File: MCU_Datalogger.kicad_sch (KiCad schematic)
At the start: 25 parts, among them U1 24LC1025, U2 DS1337S_, U3 24LC1025, U4 ATMEGA328P-AU, Y1 32.768 KHz, Y2 16MHz

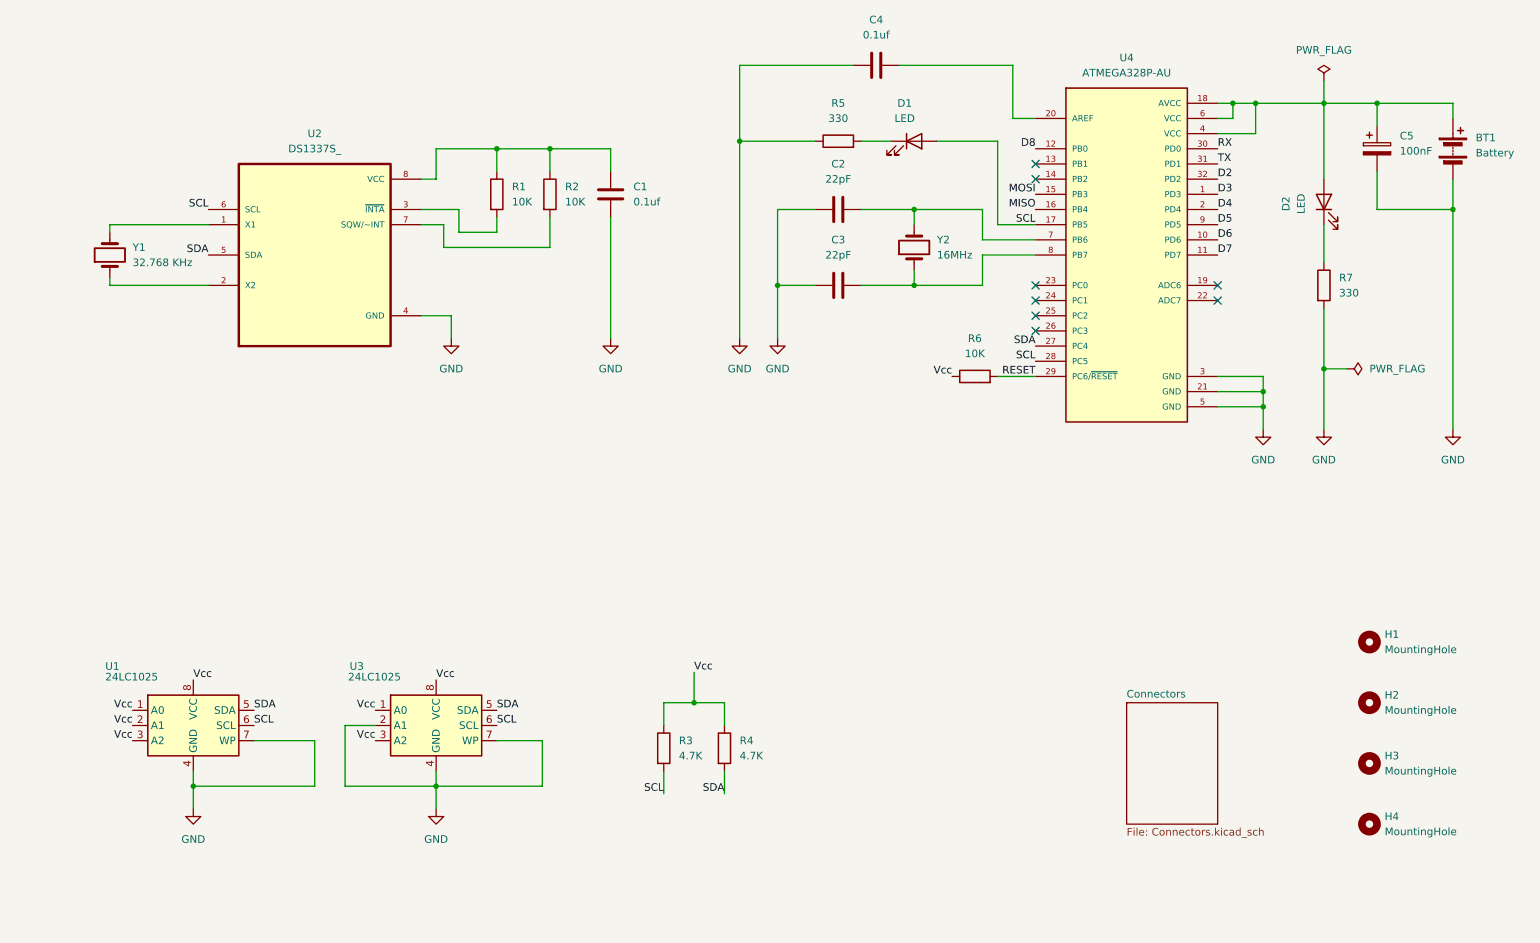
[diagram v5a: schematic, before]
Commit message: Complete wiring in second Sch
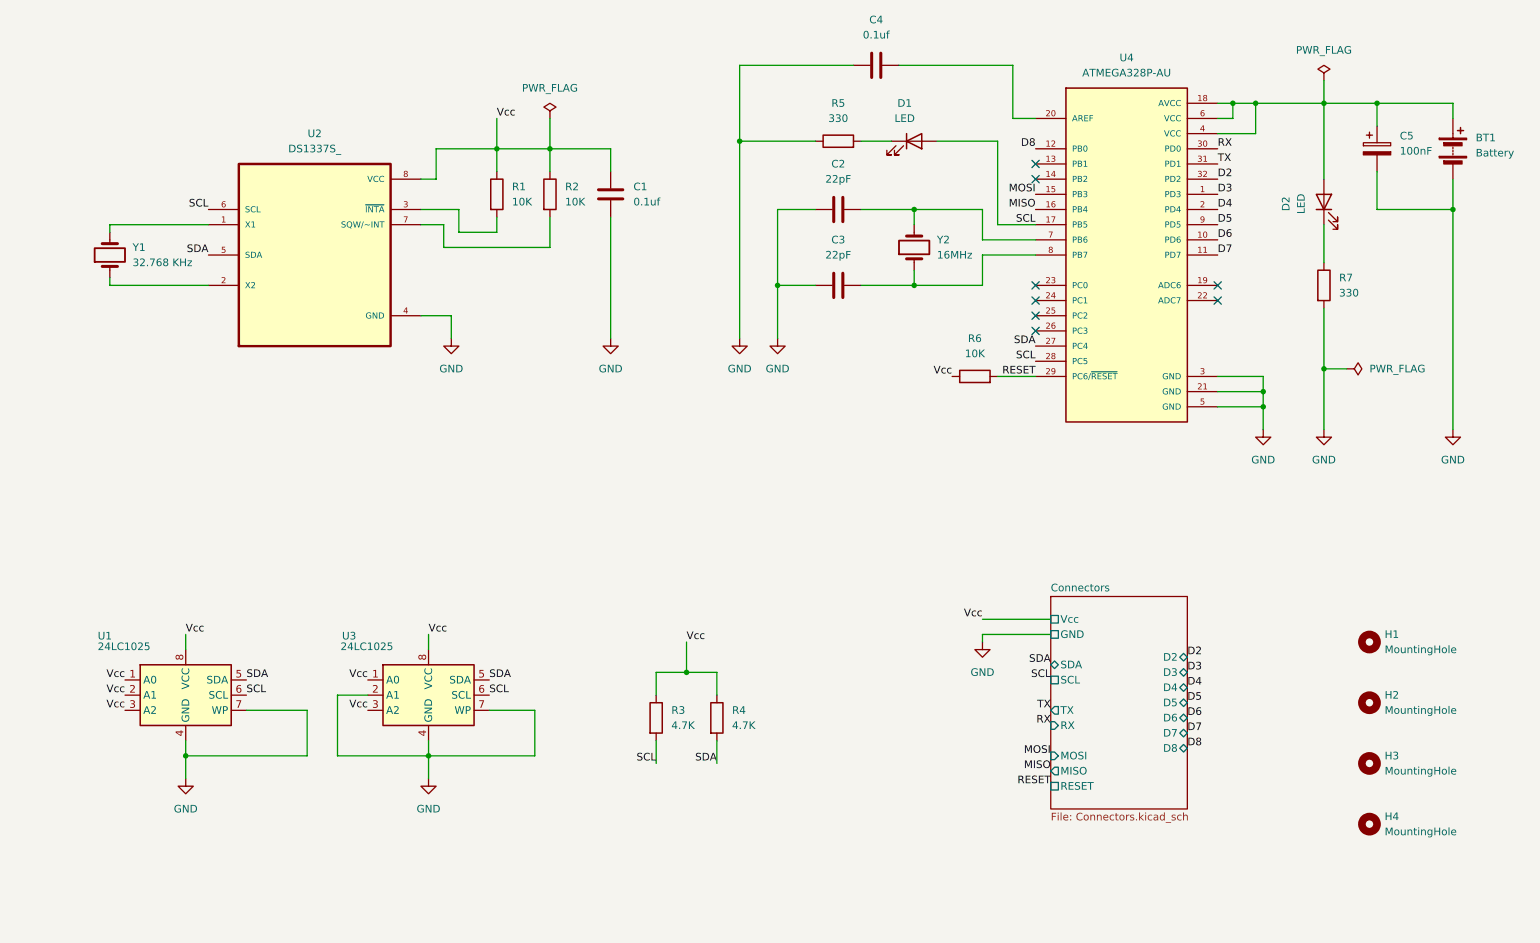
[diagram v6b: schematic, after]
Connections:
- net Vcc: now also C1.1, R1.1, R2.1, U2.8 (VCC)
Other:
- sheet Connectors ports: added D2, D3, D4, D5, D6, D7, D8, GND, MISO, MOSI, RESET, RX, SCL, SDA, TX, Vcc; removed none
- moved on the sheet: R3, R4, U1, U3
